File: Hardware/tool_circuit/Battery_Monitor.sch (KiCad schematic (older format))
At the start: 1 part

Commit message: Pi hat
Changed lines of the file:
@@
 $Descr A4 11693 8268
 encoding utf-8
-Sheet 3 5
+Sheet 3 6
 Title ""
 Date ""
@@
 Comment4 ""
 $EndDescr
-Text HLabel 4600 3100 0    50   BiDi ~ 0
+Text HLabel 5050 3200 0    50   BiDi ~ 0
 BATT_MON_DATA
 $Comp

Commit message: regulator/other changes
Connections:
- net GND: now reaches U?.6 (CTG)
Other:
- moved on the sheet: U?
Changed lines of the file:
@@
 $Descr A4 11693 8268
 encoding utf-8
-Sheet 3 6
+Sheet 3 7
 Title ""
 Date ""
@@
 L Battery_Management:DS2745U U?
 U 1 1 611EC761
-P 7400 3450
+P 6650 3450
 AR Path="/611EC761" Ref="U?"  Part="1"
 AR Path="/611DF2F9/611EC761" Ref="U?"  Part="1"
-F 0 "U?" H 7400 3931 50  0000 C CNN
-F 1 "DS2745U" H 7400 3840 50  0000 C CNN
-F 2 "Package_SO:TSSOP-8_3x3mm_P0.65mm" H 7400 2950 50  0001 C CNN
-F 3 "https://datasheets.maximintegrated.com/en/ds/DS2745.pdf" H 7500 3050 50  0001 C CNN
-	1    7400 3450
+F 0 "U?" H 6650 3931 50  0000 C CNN
+F 1 "DS2745U" H 6650 3840 50  0000 C CNN
+F 2 "Package_SO:TSSOP-8_3x3mm_P0.65mm" H 6650 2950 50  0001 C CNN
+F 3 "https://datasheets.maximintegrated.com/en/ds/DS2745.pdf" H 6750 3050 50  0001 C CNN
+	1    6650 3450
 	1    0    0    -1
 $EndComp
@@
 L power:+BATT #PWR?
 U 1 1 611ED520
-P 8300 3050
-F 0 "#PWR?" H 8300 2900 50  0001 C CNN
-F 1 "+BATT" H 8315 3223 50  0000 C CNN
-F 2 "" H 8300 3050 50  0001 C CNN
-F 3 "" H 8300 3050 50  0001 C CNN
-	1    8300 3050
+P 7550 3050
+F 0 "#PWR?" H 7550 2900 50  0001 C CNN
+F 1 "+BATT" H 7565 3223 50  0000 C CNN
+F 2 "" H 7550 3050 50  0001 C CNN
+F 3 "" H 7550 3050 50  0001 C CNN
+	1    7550 3050
 	1    0    0    -1
 $EndComp
 Wire Wire Line
-	8300 3050 8300 3350
+	7550 3050 7550 3350
 Wire Wire Line
-	8300 3350 7800 3350
+	7550 3350 7050 3350
+$Comp
+L power:GND #PWR?
+U 1 1 612D54EC
+P 7250 3750
+F 0 "#PWR?" H 7250 3500 50  0001 C CNN
+F 1 "GND" H 7255 3577 50  0000 C CNN
+F 2 "" H 7250 3750 50  0001 C CNN
+F 3 "" H 7250 3750 50  0001 C CNN
+	1    7250 3750
+	1    0    0    -1
+$EndComp
+Wire Wire Line
+	7050 3650 7250 3650
+Wire Wire Line
+	7250 3650 7250 3750
 $EndSCHEMATC

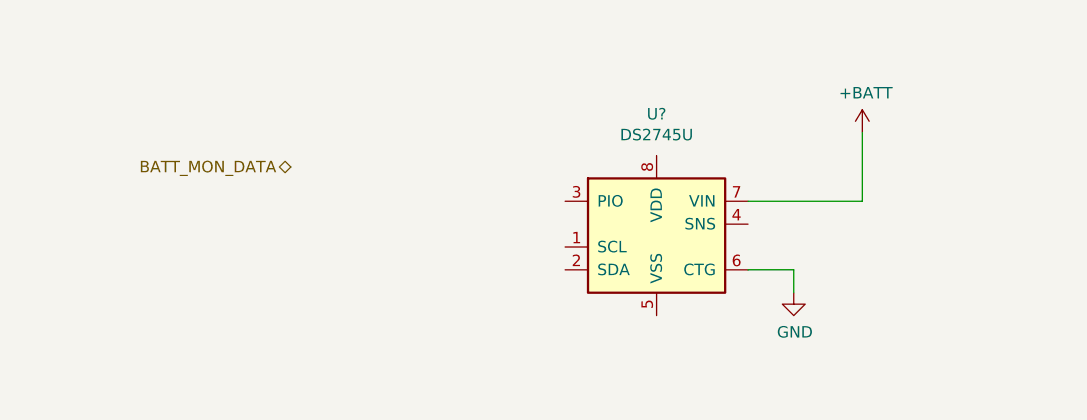
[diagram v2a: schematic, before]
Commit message: 5v regulator
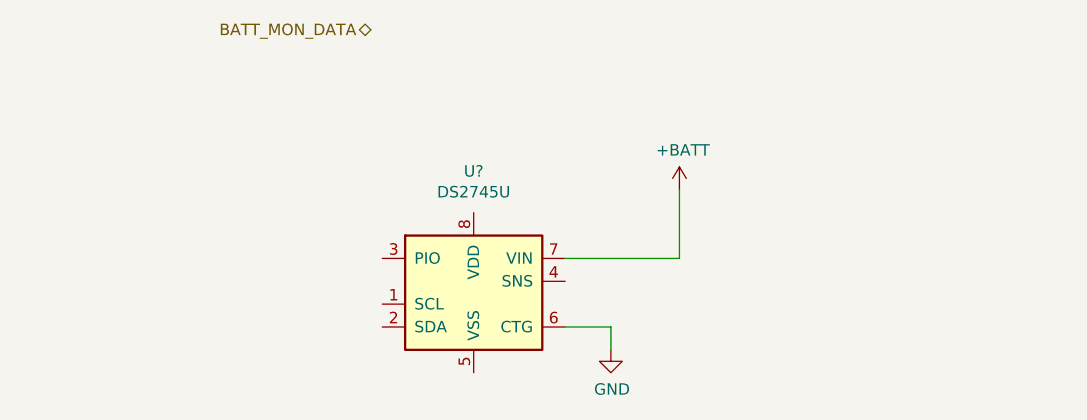
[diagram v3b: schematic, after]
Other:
- moved on the sheet: U?
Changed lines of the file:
@@
 Comment4 ""
 $EndDescr
-Text HLabel 5050 3200 0    50   BiDi ~ 0
+Text HLabel 5400 2600 0    50   BiDi ~ 0
 BATT_MON_DATA
 $Comp
 L Battery_Management:DS2745U U?
 U 1 1 611EC761
-P 6650 3450
+P 5850 3700
 AR Path="/611EC761" Ref="U?"  Part="1"
 AR Path="/611DF2F9/611EC761" Ref="U?"  Part="1"
-F 0 "U?" H 6650 3931 50  0000 C CNN
-F 1 "DS2745U" H 6650 3840 50  0000 C CNN
-F 2 "Package_SO:TSSOP-8_3x3mm_P0.65mm" H 6650 2950 50  0001 C CNN
-F 3 "https://datasheets.maximintegrated.com/en/ds/DS2745.pdf" H 6750 3050 50  0001 C CNN
-	1    6650 3450
+F 0 "U?" H 5850 4181 50  0000 C CNN
+F 1 "DS2745U" H 5850 4090 50  0000 C CNN
+F 2 "Package_SO:TSSOP-8_3x3mm_P0.65mm" H 5850 3200 50  0001 C CNN
+F 3 "https://datasheets.maximintegrated.com/en/ds/DS2745.pdf" H 5950 3300 50  0001 C CNN
+	1    5850 3700
 	1    0    0    -1
 $EndComp
@@
 L power:+BATT #PWR?
 U 1 1 611ED520
-P 7550 3050
-F 0 "#PWR?" H 7550 2900 50  0001 C CNN
-F 1 "+BATT" H 7565 3223 50  0000 C CNN
-F 2 "" H 7550 3050 50  0001 C CNN
-F 3 "" H 7550 3050 50  0001 C CNN
-	1    7550 3050
+P 6750 3300
+F 0 "#PWR?" H 6750 3150 50  0001 C CNN
+F 1 "+BATT" H 6765 3473 50  0000 C CNN
+F 2 "" H 6750 3300 50  0001 C CNN
+F 3 "" H 6750 3300 50  0001 C CNN
+	1    6750 3300
 	1    0    0    -1
 $EndComp
 Wire Wire Line
-	7550 3050 7550 3350
+	6750 3300 6750 3600
 Wire Wire Line
-	7550 3350 7050 3350
+	6750 3600 6250 3600
 $Comp
 L power:GND #PWR?
 U 1 1 612D54EC
-P 7250 3750
-F 0 "#PWR?" H 7250 3500 50  0001 C CNN
-F 1 "GND" H 7255 3577 50  0000 C CNN
-F 2 "" H 7250 3750 50  0001 C CNN
-F 3 "" H 7250 3750 50  0001 C CNN
-	1    7250 3750
+P 6450 4000
+F 0 "#PWR?" H 6450 3750 50  0001 C CNN
+F 1 "GND" H 6455 3827 50  0000 C CNN
+F 2 "" H 6450 4000 50  0001 C CNN
+F 3 "" H 6450 4000 50  0001 C CNN
+	1    6450 4000
 	1    0    0    -1
 $EndComp
 Wire Wire Line
-	7050 3650 7250 3650
+	6250 3900 6450 3900
 Wire Wire Line
-	7250 3650 7250 3750
+	6450 3900 6450 4000
 $EndSCHEMATC
